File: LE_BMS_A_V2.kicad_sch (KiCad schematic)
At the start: 0 parts

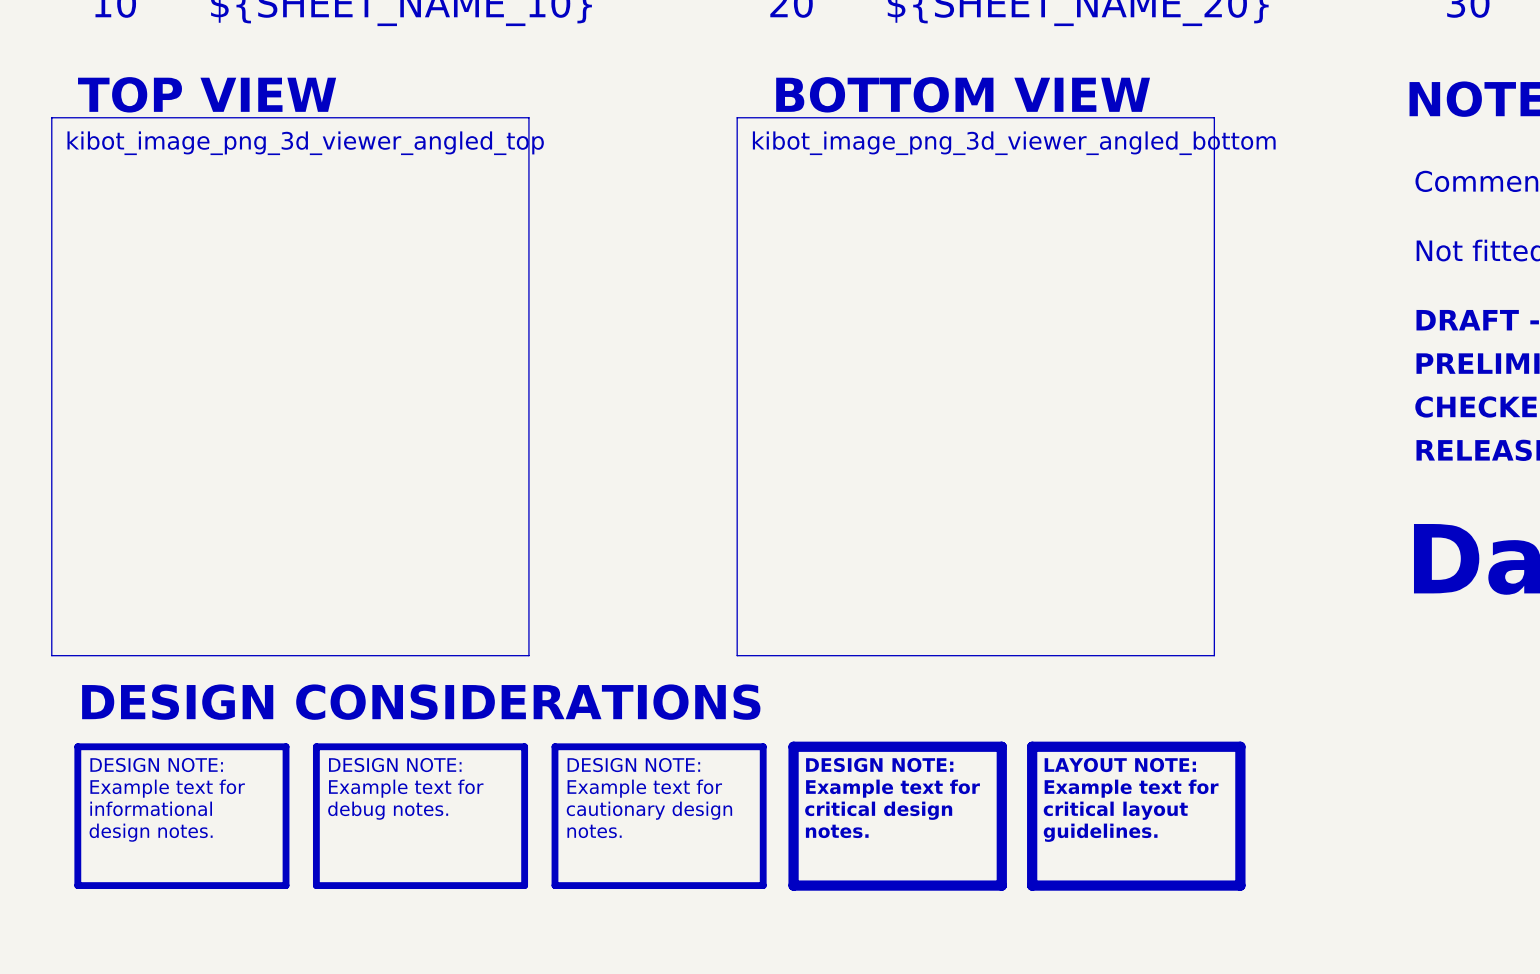
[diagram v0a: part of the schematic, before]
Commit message: Initial commit: Moved over previous design and added isolation to CAN bus.
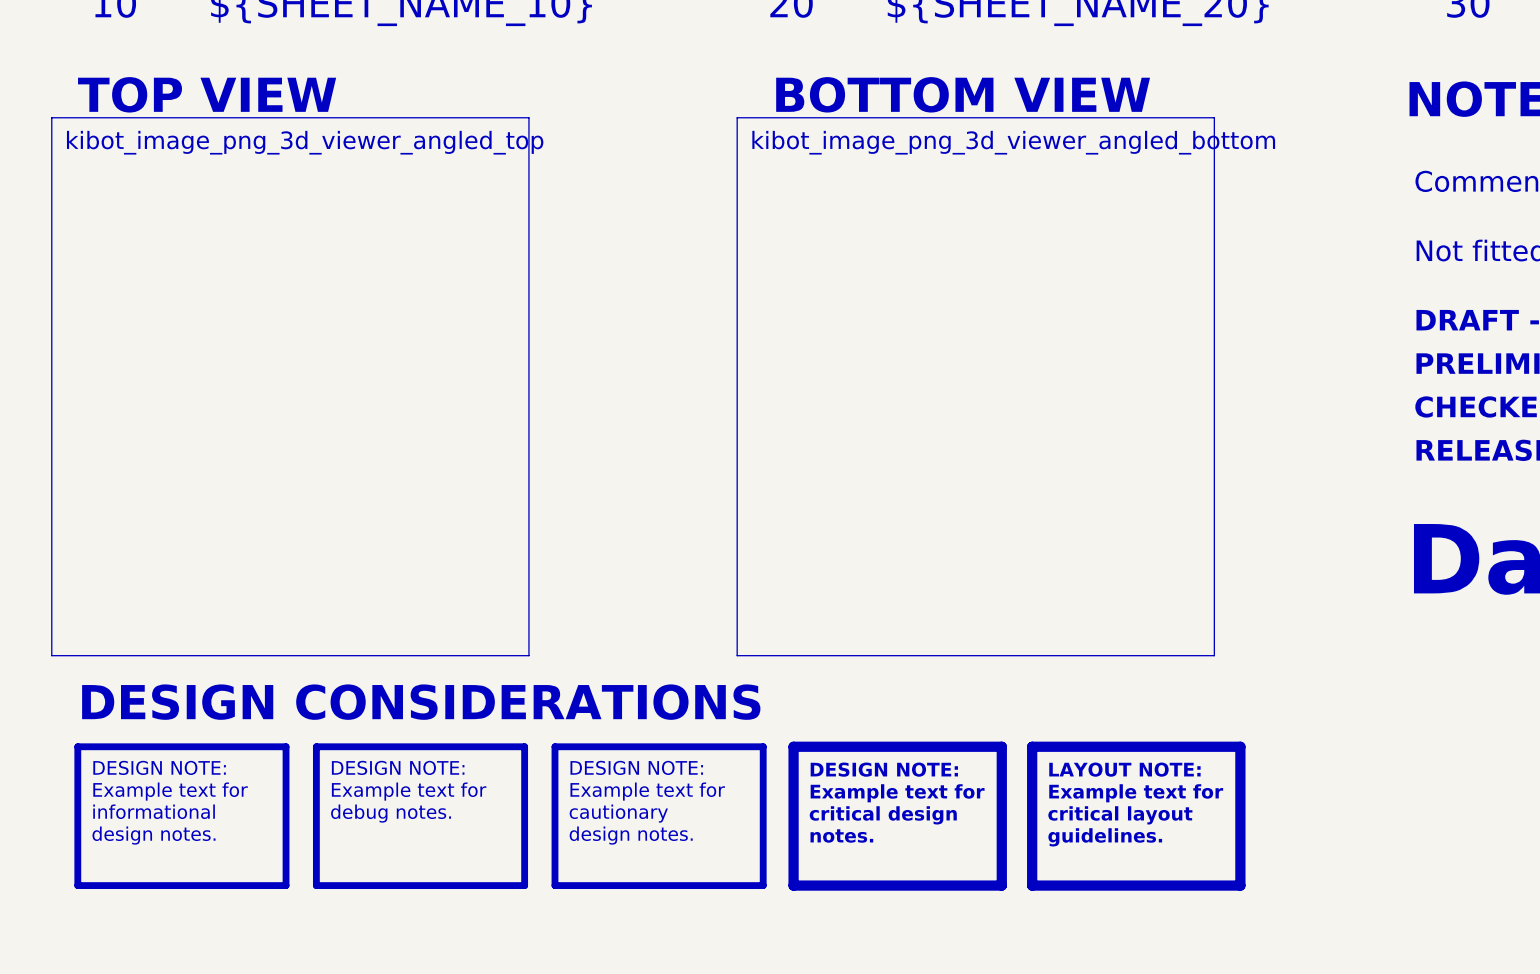
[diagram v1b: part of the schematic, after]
